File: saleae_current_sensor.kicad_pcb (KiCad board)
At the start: 4 copper layers, 64 x 40.4 mm, 44 parts, among them J1 USB4505-03-0-A_REVA, J2 TSM-104-02-T-DH, M1 MountingHole_Pad, M2 MountingHole_Pad, M3 MountingHole_Pad, U1 TES_1-0523, U2 L78L12, U3 L7912, U4 ACS723xLCTR-05AB, U5 ACS723xLCTR-40AB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

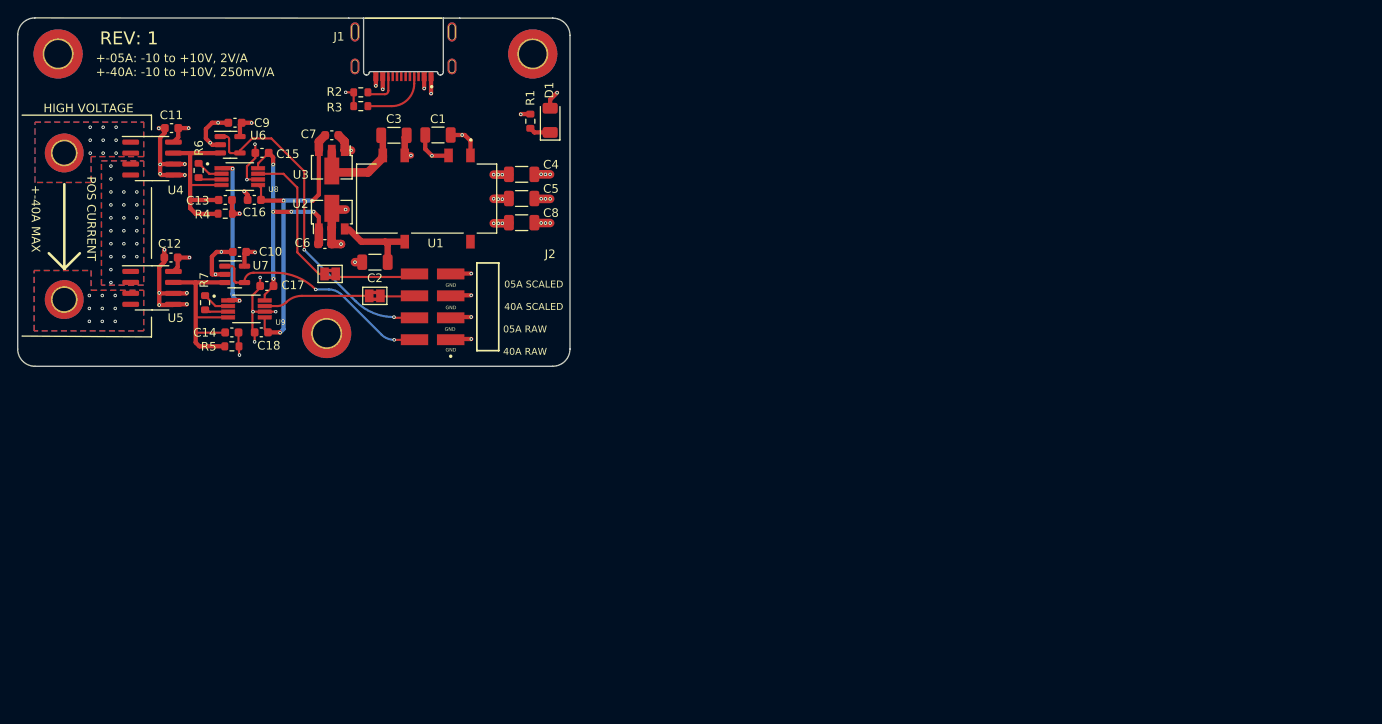
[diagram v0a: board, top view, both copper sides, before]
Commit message: Export outputs via GitHub Actions w/ KiCad CLI
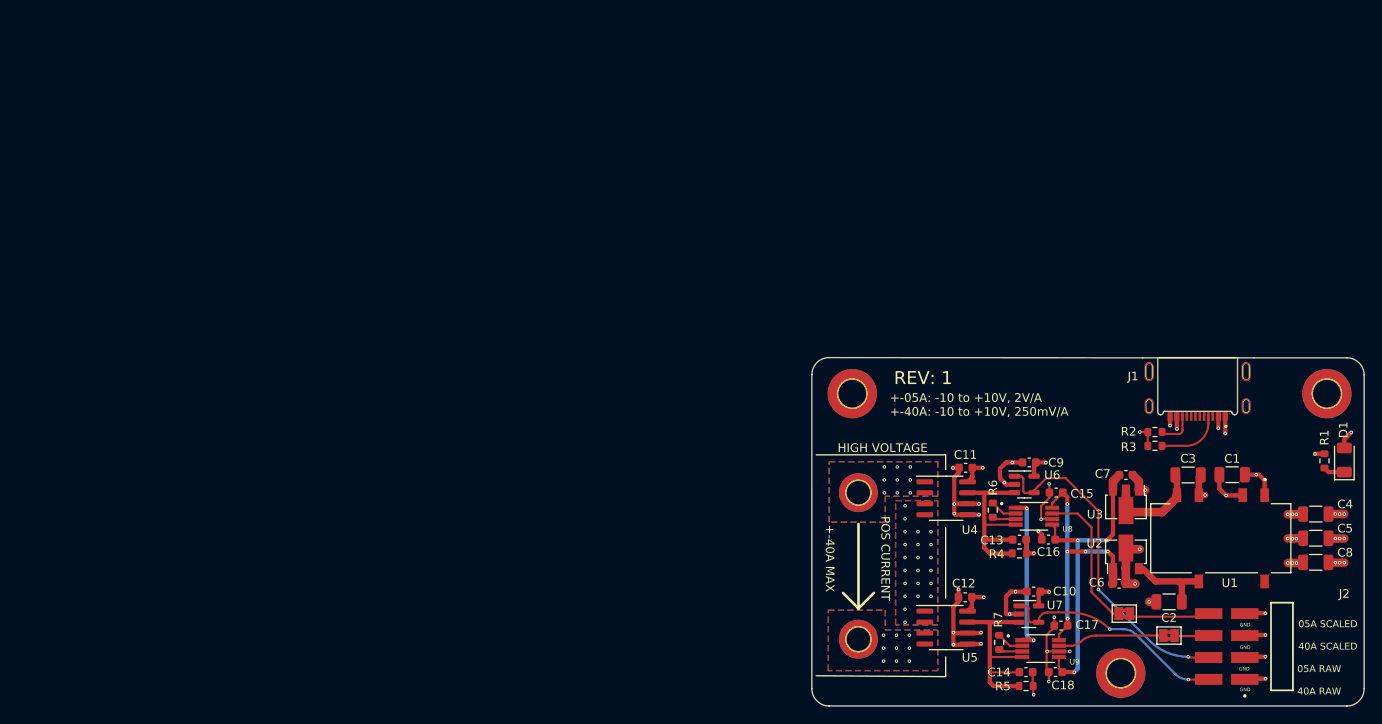
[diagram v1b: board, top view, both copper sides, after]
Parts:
- moved R6 100.1 mm to (215.0, 127.0)
- moved R7 100.1 mm to (215.7, 142.3)
- moved C1 100.1 mm to (242.7, 122.9)
- moved C14 100.1 mm to (218.8, 145.7)
- moved C15 100.1 mm to (222.3, 124.9)
- moved C16 100.1 mm to (221.4, 130.4)
- moved C17 100.1 mm to (222.9, 140.4)
- moved C18 100.1 mm to (222.3, 145.7)
- moved C2 100.1 mm to (235.4, 137.6)
- moved C3 100.1 mm to (237.6, 122.9)
- moved C4 100.1 mm to (252.4, 127.4)
- moved C5 100.1 mm to (252.4, 130.2)
- moved C6 100.1 mm to (229.6, 135.5)
- moved C7 100.1 mm to (230.4, 122.9)
- moved C8 100.1 mm to (252.4, 133.0)
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
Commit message: Misc updates kibuzzard lock in mounting holes/connectors change dielectric thickness for total 1.6mm stackup CI updates
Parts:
- added kibuzzard-64A244C5: G***, kibuzzard-64A244C5, F.Cu at (197.5, 133.2)
- added kibuzzard-64A24575: G***, kibuzzard-64A24575, F.Cu at (199.4, 133.5)
- added kibuzzard-64A2F491: G***, kibuzzard-64A2F491, B.Cu at (252.4, 146.0)
- added kibuzzard-64A2F4F2: G***, kibuzzard-64A2F4F2, F.Cu at (202.0, 119.1)
- added kibuzzard-64A2F4F7: G***, kibuzzard-64A2F4F7, F.Cu at (202.0, 147.7)
- R6, R7: value 4.95K -> 5K
- U3: value L7912 -> L79L12
- moved M1 0.85 mm to (198.0, 113.0)
- moved M2 0.55 mm to (254.0, 113.0)
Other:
- board text removed: "HIGH VOLTAGE"
- board text removed: "POS CURRENT +-40A MAX"

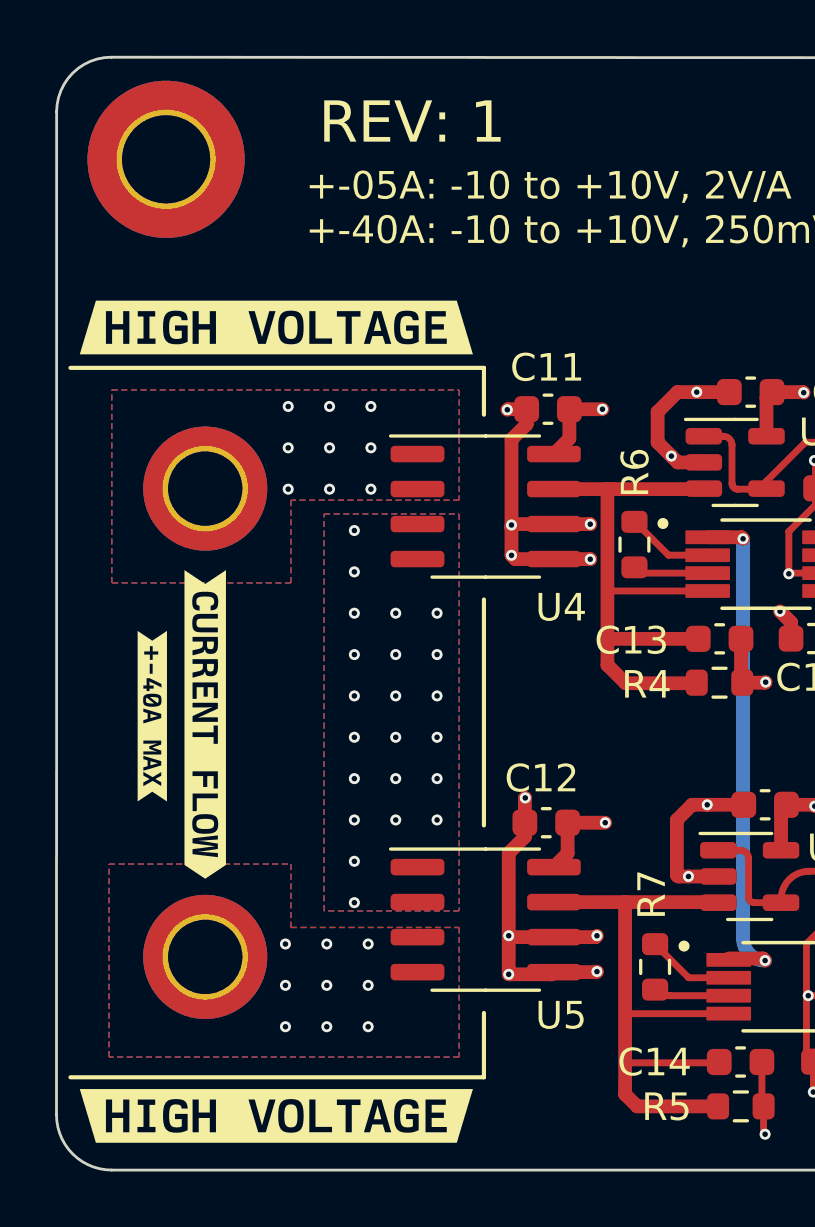
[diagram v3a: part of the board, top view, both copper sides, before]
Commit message: Route a gap between LV and HV sides of current sensors
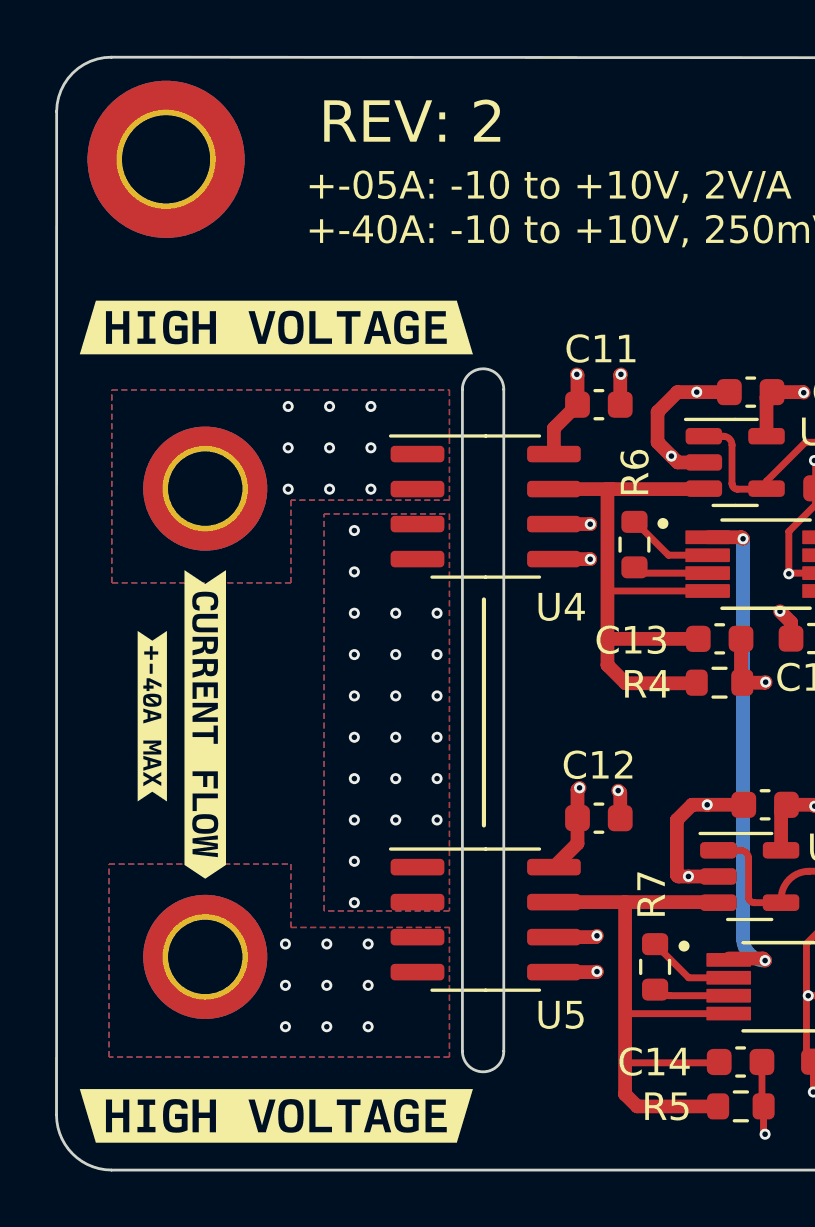
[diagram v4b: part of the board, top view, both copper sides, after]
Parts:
- moved C12 1.92 mm to (213.7, 136.9), turned to 0 degrees
- moved C11 1.85 mm to (213.7, 121.9), turned to 0 degrees
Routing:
- net GND: track 100.8 -> 103.4 mm, vias 46 -> 42
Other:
- outline, holes or cut-outs redrawn

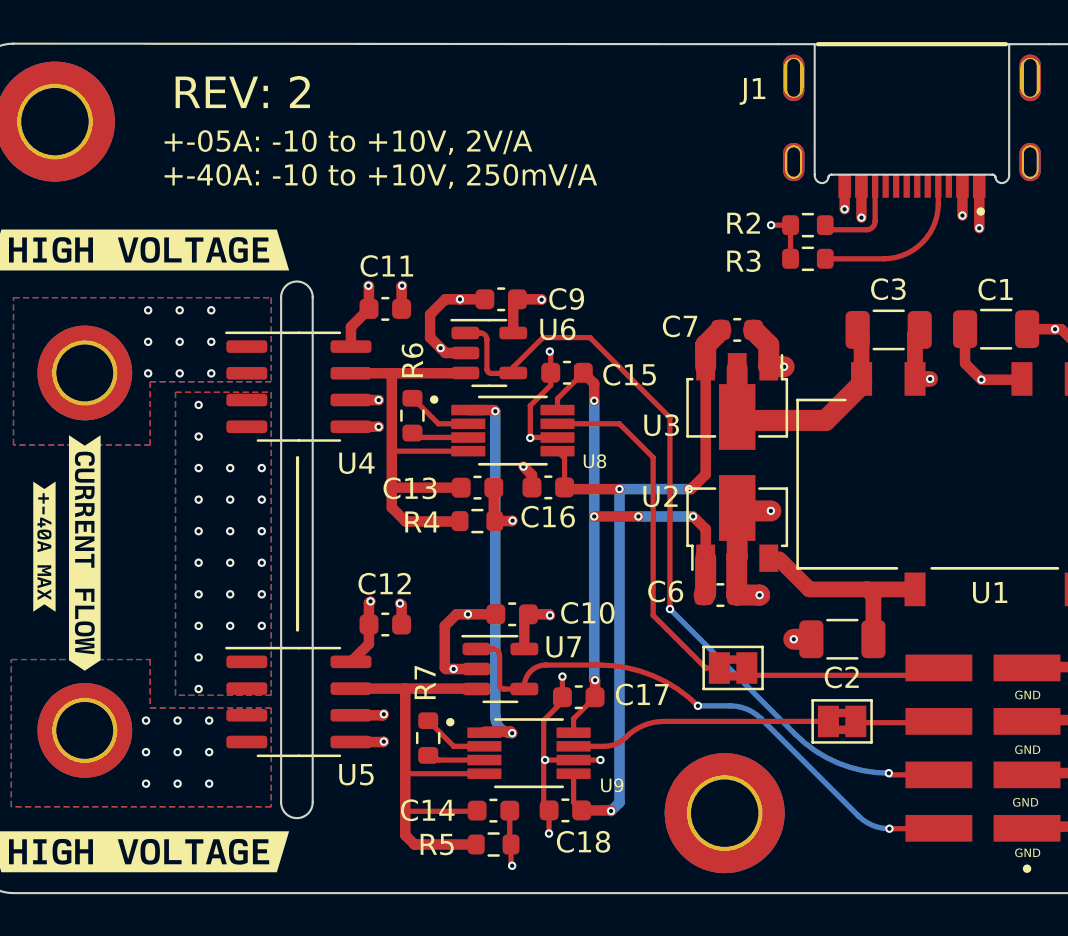
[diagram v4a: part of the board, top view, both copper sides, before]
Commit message: Add 2V5 voltage reference :( and reduce LED resistor
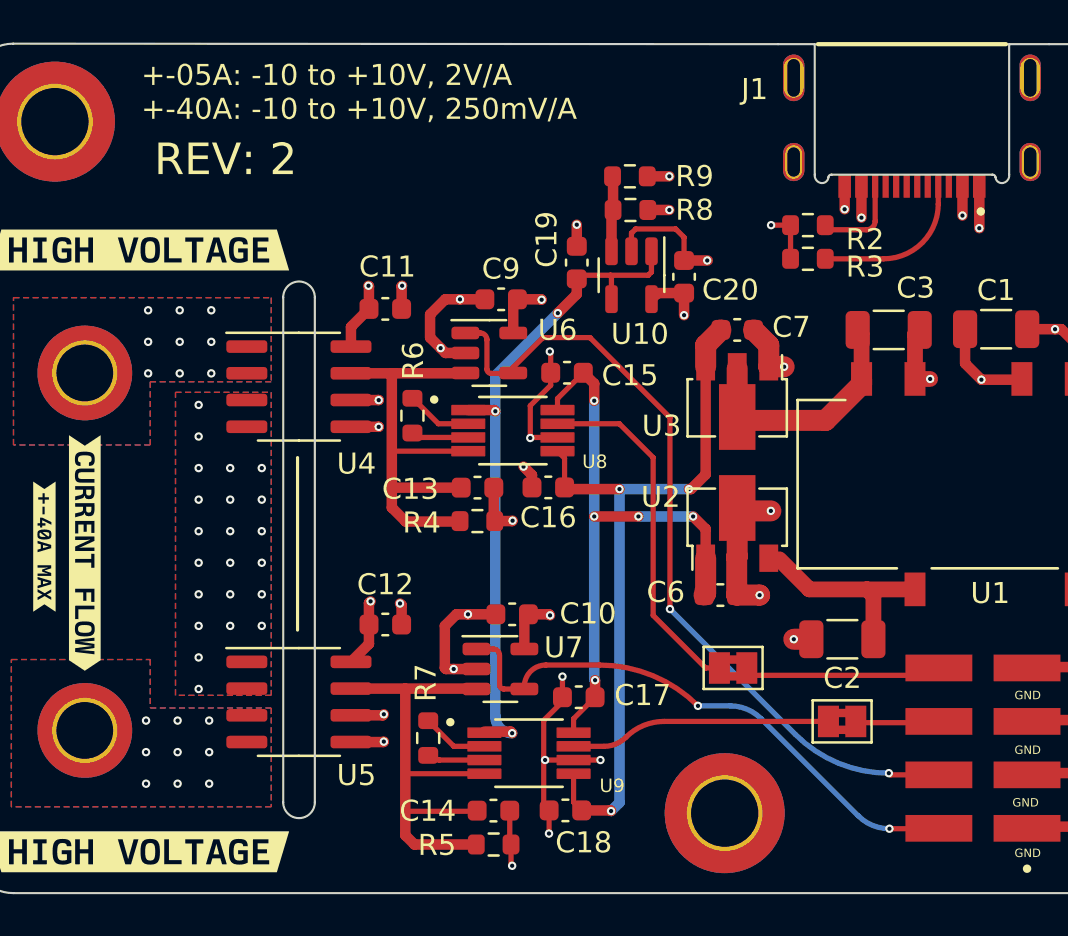
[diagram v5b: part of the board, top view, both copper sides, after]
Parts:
- added C19: 100nF, Capacitor_SMD:C_0603_1608Metric, F.Cu at (222.8, 119.7)
- added C20: 100nF, Capacitor_SMD:C_0603_1608Metric, F.Cu at (227.9, 120.4)
- added R8: 1K, Resistor_SMD:R_0603_1608Metric, F.Cu at (225.3, 117.2)
- added R9: 1K, Resistor_SMD:R_0603_1608Metric, F.Cu at (225.3, 115.6)
- added U10: LT6015xS5, Package_TO_SOT_SMD:SOT-23-5, F.Cu at (225.4, 120.3)
- R1: value 2.5K -> 200
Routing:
- net +2V5: track 18.4 -> 32.1 mm, vias 2 -> 3
- net GND: track 103.4 -> 111.3 mm, vias 42 -> 45
- net +5V: track 27.3 -> 31.0 mm, vias 17 -> 19
- net Net-(U10-+): track 0.00 -> 3.60 mm
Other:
- outline, holes or cut-outs redrawn
